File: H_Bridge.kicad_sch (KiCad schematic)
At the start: 12 parts, among them IC1 BD64950EFJ-E2, IC2 BD64950EFJ-E2, IC3 BD64950EFJ-E2, IC4 BD64950EFJ-E2, IC5 BD64950EFJ-E2, IC6 BD64950EFJ-E2

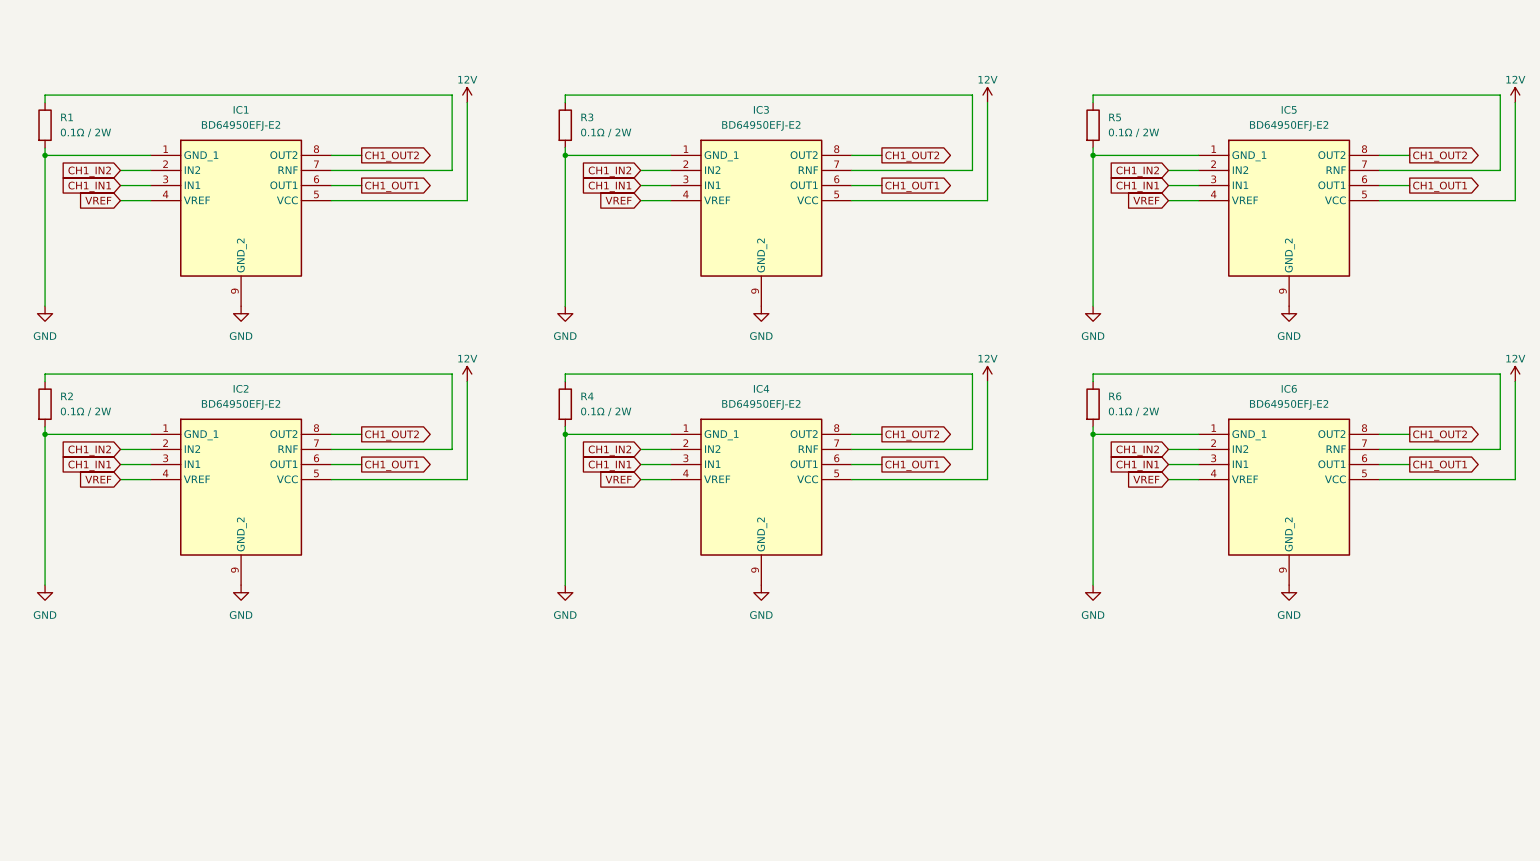
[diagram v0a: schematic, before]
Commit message: create 6ch H-Bridgies
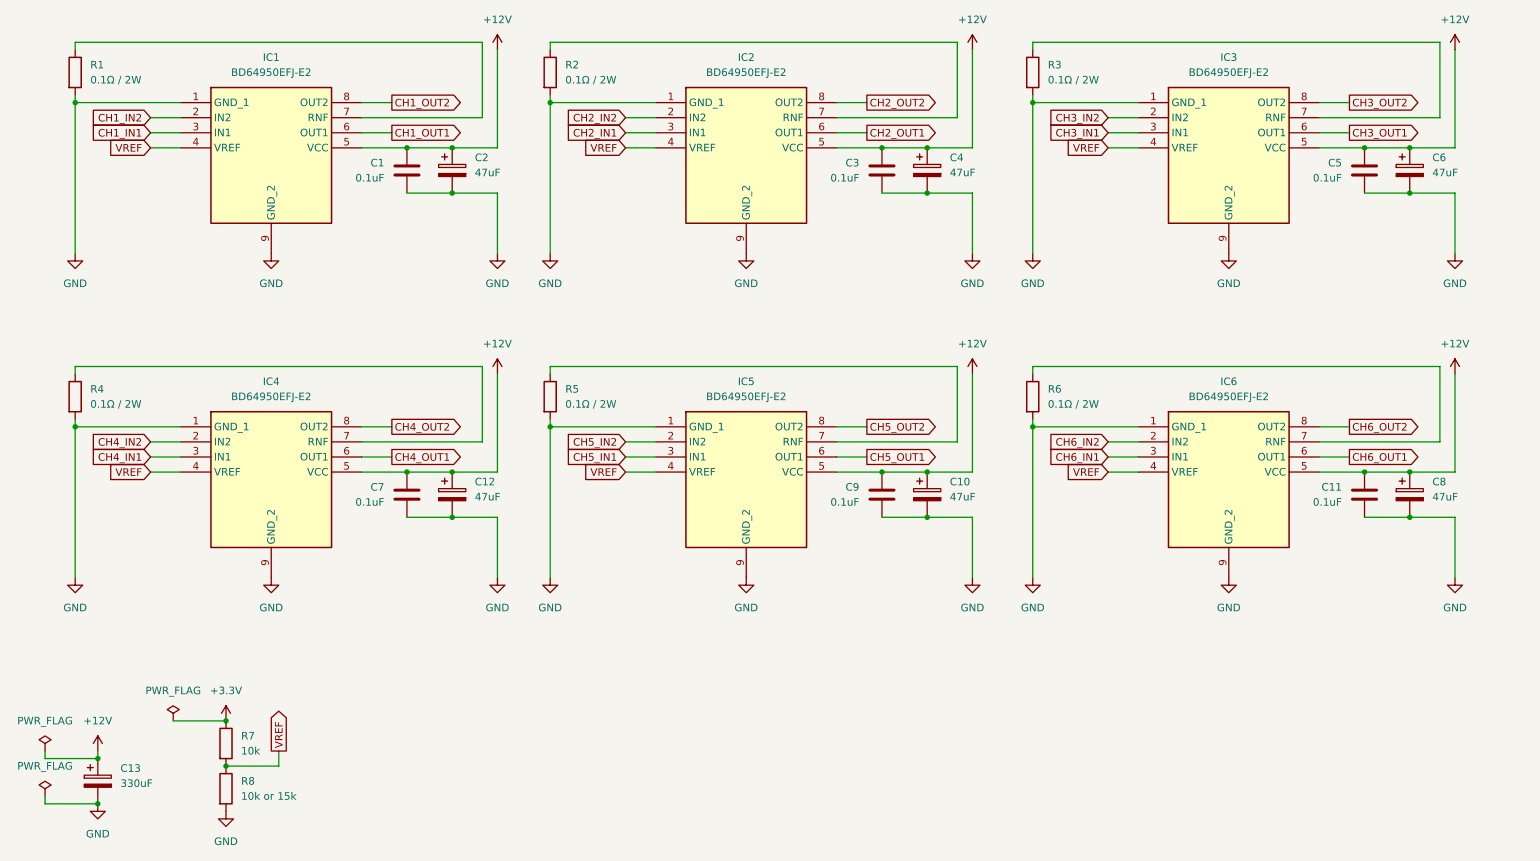
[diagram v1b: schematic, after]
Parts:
- added C1, C11, C3, C5, C7, C9: 0.1uF, Capacitor_SMD:C_0603_1608Metric_Pad1.08x0.95mm_HandSolder, symbol Device:C
- added C10, C12, C2, C4, C6, C8: 47uF, Capacitor_SMD:CP_Elec_6.3x7.7, symbol Device:C_Polarized
- added C13: 330uF, Capacitor_SMD:CP_Elec_10x10.5, symbol Device:C_Polarized
- added R7: 10k, Resistor_SMD:R_0603_1608Metric_Pad0.98x0.95mm_HandSolder, symbol Device:R
- added R8: 10k or 15k, Resistor_SMD:R_0603_1608Metric_Pad0.98x0.95mm_HandSolder, symbol Device:R
- IC1, IC2, IC3, IC4, IC5, IC6: footprint SOIC127P600X100-9N -> HTSOP-J8_footprint_symbol:HTSOP-J8
- R1, R2, R3, R4, R5, R6: footprint Resistor_SMD:R_0603_1608Metric_Pad0.98x0.95mm_HandSolder -> Resistor_SMD:R_2512_6332Metric_Pad1.40x3.35mm_HandSolder; EC (none) -> LCSC; MPN (none) -> RVR HIXD25LR100J; Part Number (none) -> C53144937
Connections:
- net CH1_IN1: no longer IC2.3 (IN1), IC3.3 (IN1), IC4.3 (IN1), IC5.3 (IN1), IC6.3 (IN1)
- net CH1_IN2: no longer IC2.2 (IN2), IC3.2 (IN2), IC4.2 (IN2), IC5.2 (IN2), IC6.2 (IN2)
- net CH1_OUT1: no longer IC2.6 (OUT1), IC3.6 (OUT1), IC4.6 (OUT1), IC5.6 (OUT1), IC6.6 (OUT1)
- net CH1_OUT2: no longer IC2.8 (OUT2), IC3.8 (OUT2), IC4.8 (OUT2), IC5.8 (OUT2), IC6.8 (OUT2)
- net GND: now also C1.2, C10.2, C11.2, C12.2, C13.2, C2.2, C3.2, C4.2, C5.2, C6.2, C7.2, C8.2, C9.2, R8.2
- net VREF: now also R7.2, R8.1
- net 12V renamed +12V
- net +12V: now also C1.1, C10.1, C11.1, C12.1, C13.1, C2.1, C3.1, C4.1, C5.1, C6.1, C7.1, C8.1, C9.1
- new net +3.3V: R7.1
- new net CH2_IN1: IC2.3 (IN1)
- new net CH2_IN2: IC2.2 (IN2)
- new net CH2_OUT1: IC2.6 (OUT1)
- new net CH2_OUT2: IC2.8 (OUT2)
- new net CH3_IN1: IC3.3 (IN1)
- new net CH3_IN2: IC3.2 (IN2)
- new net CH3_OUT1: IC3.6 (OUT1)
- new net CH3_OUT2: IC3.8 (OUT2)
- new net CH4_IN1: IC4.3 (IN1)
- new net CH4_IN2: IC4.2 (IN2)
- new net CH4_OUT1: IC4.6 (OUT1)
- new net CH4_OUT2: IC4.8 (OUT2)
- new net CH5_IN1: IC5.3 (IN1)
- new net CH5_IN2: IC5.2 (IN2)
- new net CH5_OUT1: IC5.6 (OUT1)
- new net CH5_OUT2: IC5.8 (OUT2)
- new net CH6_IN1: IC6.3 (IN1)
- new net CH6_IN2: IC6.2 (IN2)
- new net CH6_OUT1: IC6.6 (OUT1)
- new net CH6_OUT2: IC6.8 (OUT2)
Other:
- moved on the sheet: IC1, R1

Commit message: update: file move
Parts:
- IC1, IC2, IC3, IC4, IC5, IC6: footprint HTSOP-J8_footprint_symbol:HTSOP-J8 -> HTSOP-J8:HTSOP-J8
